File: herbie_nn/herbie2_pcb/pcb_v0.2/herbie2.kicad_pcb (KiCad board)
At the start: 2 copper layers, 119.4 x 96.5 mm, 115 parts, among them J1 GND, J10 LEFT_ENC, J11 RIGHT_ENC, J12 Vin, J13 Conn_02x04_Odd_Even, J14 AM_Right, J15 Conn_01x03_Male, J16 Power, J17 Conn_01x03, J18 SmartPort, J19 Conn_01x04_Female, J2 5V, J20 Conn_01x03, J21 Conn_01x04_Female, J22 Conn_01x01, J3 I2C_QWIIC, J4 AM_Left, J5 Conn_01x03_Female, J6 RC_UART, J7 DOME_ENC, J8 I2C_QWIIC, J9 I2C_QWIIC, Q1 LTC4412, Q2 2N7002, Q3 Si4427, Q5 2N7002, U1 LS7366R, U2 74164, U3 24v13_Pololu, U4 LS7366R, U5 LS7366R, U6 TCA9534, U7 24v13_Pololu, U8 D36V50F5_Pololu, U9 TCA9534, Y1 20MHz, Y2 20MHz, Y3 20MHz

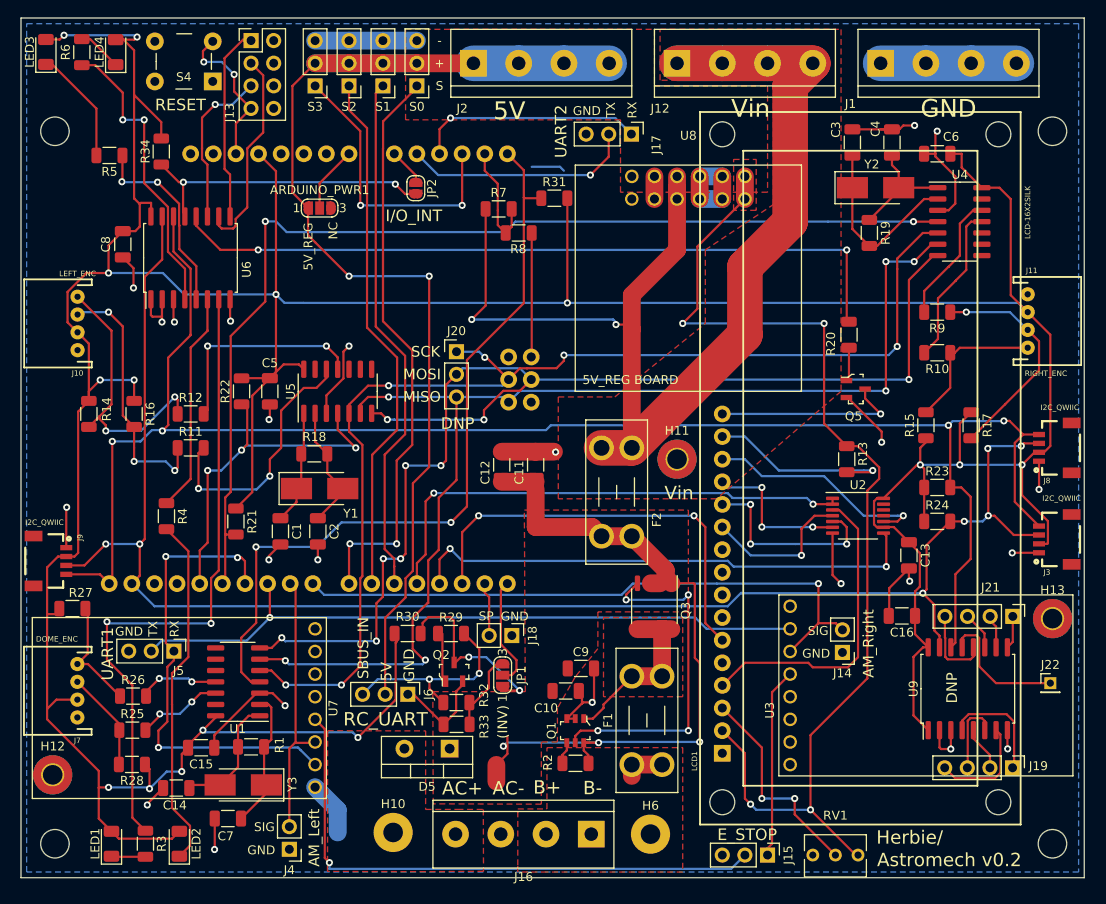
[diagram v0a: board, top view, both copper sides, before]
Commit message: added 1K resistor
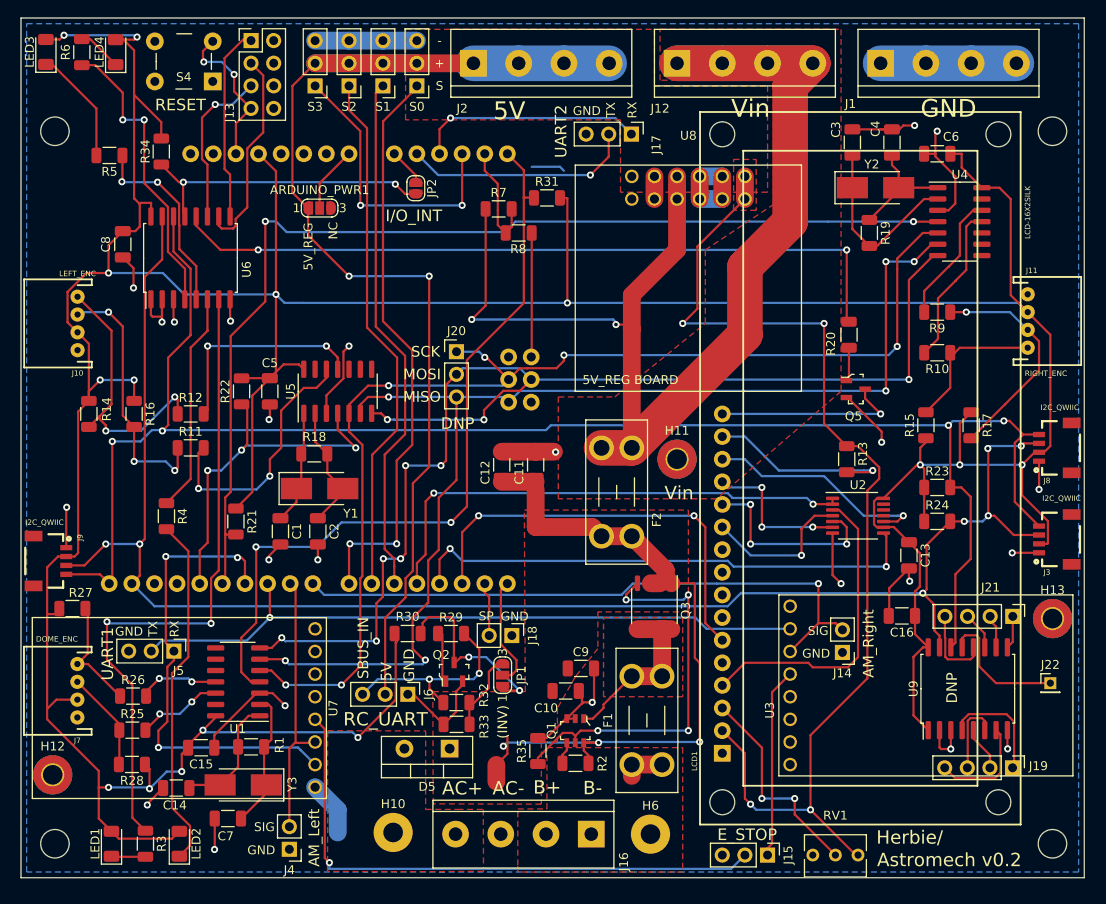
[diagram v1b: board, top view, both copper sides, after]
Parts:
- added R35: 1K, Resistor_SMD:R_1206_3216Metric, F.Cu at (160.9, 121.7)
- moved R31 0.83 mm to (161.9, 59.6)
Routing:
- net Net-(Q1-Pad5): track 38.5 -> 44.7 mm
- net GND: track 194.4 -> 198.5 mm
- net 3.3V: track 489.0 -> 489.9 mm
- net ENC3_SS: track 87.9 -> 87.1 mm
